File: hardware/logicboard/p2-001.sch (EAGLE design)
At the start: 59 parts, among them IC1 74LS07N, IC11 74LS153D, IC12 LTC485S, IC13 LTC485S, IC2 4066N, J1 MKR, J11 Qwiic, J12 Qwiic, J13 Qwiic, J14 Qwiic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

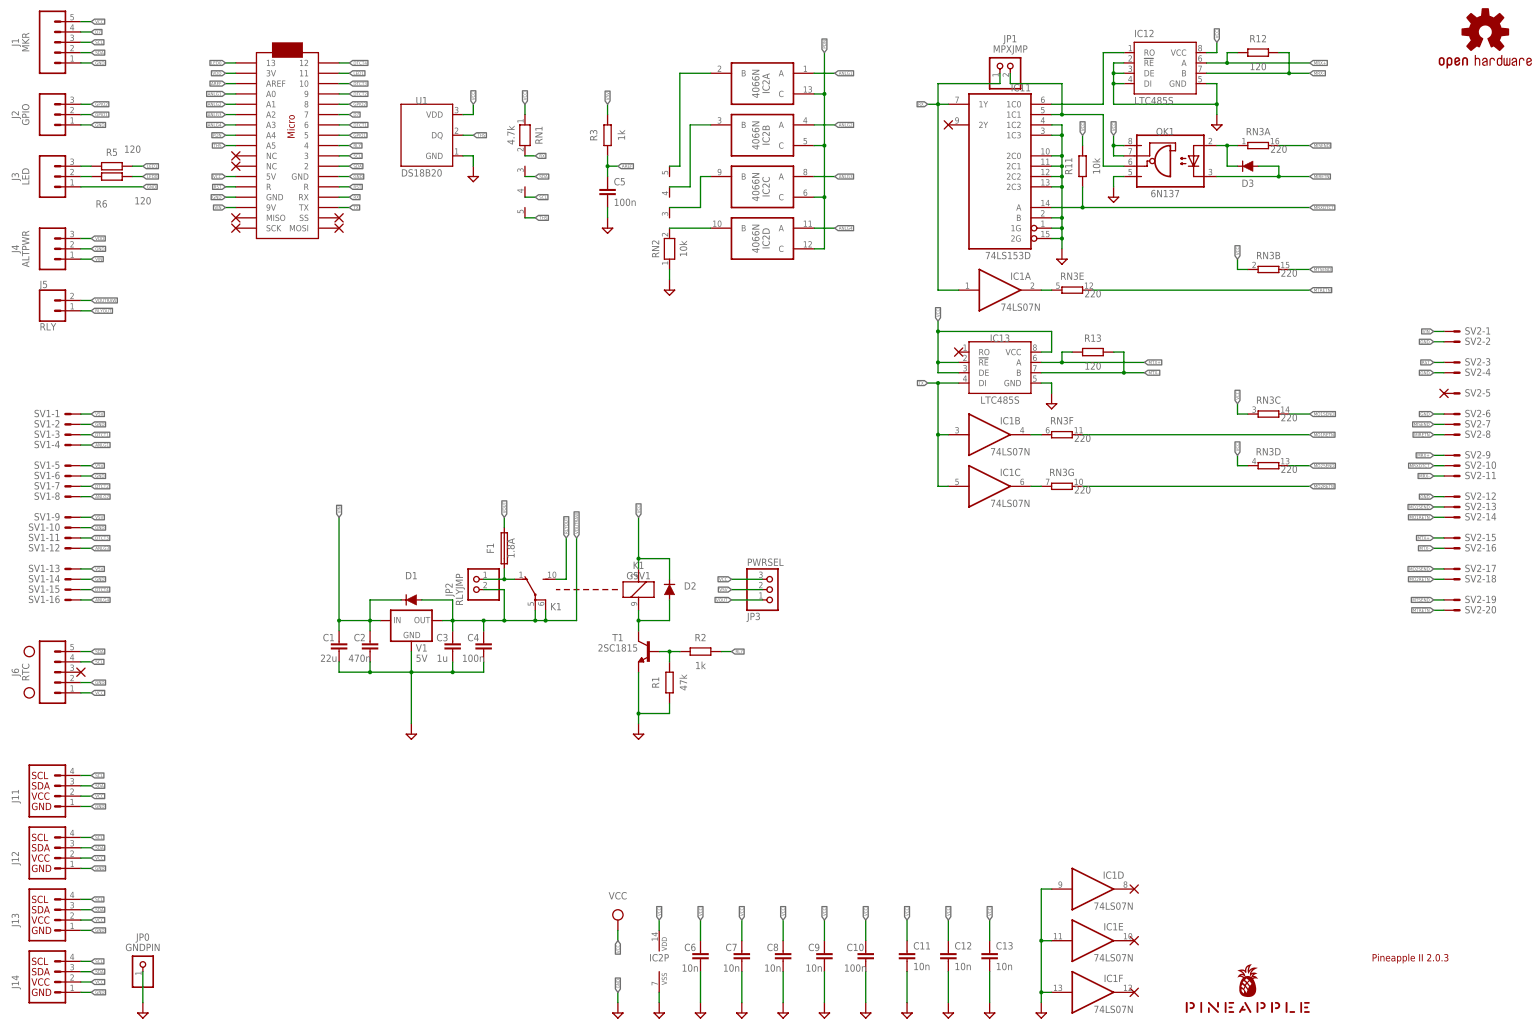
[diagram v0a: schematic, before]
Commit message: Added Power-Grid.
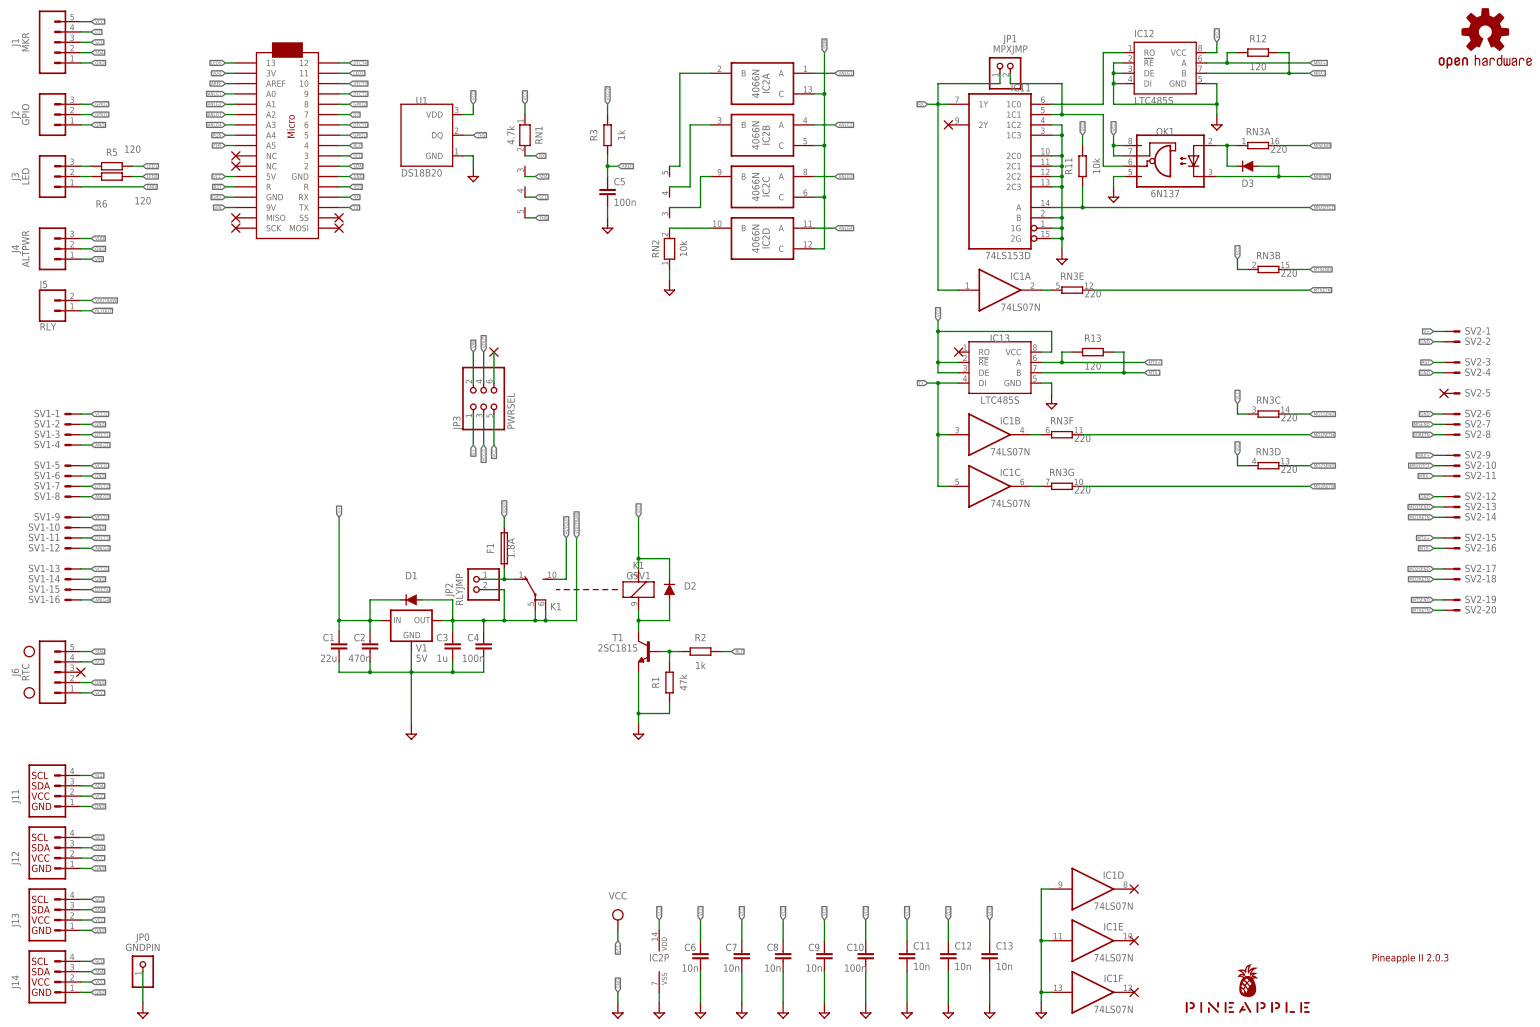
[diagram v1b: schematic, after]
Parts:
- JP3: device pinhead:PINHD-1X3 -> pinhead:PINHD-2X3
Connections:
- removed net V5V: JP3.2, R3.2, SV1-1.S, SV1-13.S, SV1-5.S, SV1-9.S
- new net N$11: JP3.6
- new net V+: C1.1, C2.1, D1.C, JP3.1, SV2-1.S, V1.IN
- new net VCC/2: JP3.3, R3.2, SV1-1.S, SV1-13.S, SV1-5.S, SV1-9.S
- net VCC: now also JP3.5; no longer JP3.3
- net VIN: now also JP3.2; no longer C1.1, C2.1, D1.C, SV2-1.S, V1.IN
- net VOUT: now also JP3.4; no longer JP3.1
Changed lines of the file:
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@@
 <part name="SUPPLY5" library="supply2" library_urn="urn:adsk.eagle:library:372" deviceset="VCC" device=""/>
 <part name="X14" library="wirepad" library_urn="urn:adsk.eagle:library:412" deviceset="PAD-N" device=""/>
-<part name="JP3" library="pinhead" library_urn="urn:adsk.eagle:library:325" deviceset="PINHD-1X3" device="" package3d_urn="urn:adsk.eagle:package:22458/2" value="PWRSEL"/>
 <part name="J5" library="SparkFun-Connectors" library_urn="urn:adsk.eagle:library:513" deviceset="CONN_02" device="JST-PTH-2" package3d_urn="urn:adsk.eagle:package:38053/1" value="RLY"/>
+<part name="JP3" library="pinhead" library_urn="urn:adsk.eagle:library:325" deviceset="PINHD-2X3" device="" package3d_urn="urn:adsk.eagle:package:22462/2" value="PWRSEL"/>
+<part name="X11" library="wirepad" library_urn="urn:adsk.eagle:library:412" deviceset="PAD-N" device=""/>
 </parts>
 <sheets>
@@
 </instance>
 <instance part="X14" gate="G$1" x="25.4" y="91.44" smashed="yes"/>
-<instance part="JP3" gate="A" x="195.58" y="111.76" smashed="yes" rot="MR180">
-<attribute name="NAME" x="189.23" y="106.045" size="1.778" layer="95" rot="MR180"/>
-<attribute name="VALUE" x="189.23" y="119.38" size="1.778" layer="96" rot="MR180"/>
-</instance>
 <instance part="J5" gate="G$1" x="17.78" y="180.34" smashed="yes">
 <attribute name="VALUE" x="15.24" y="175.514" size="1.778" layer="96" font="vector"/>
 <attribute name="NAME" x="15.24" y="185.928" size="1.778" layer="95" font="vector"/>
 </instance>
+<instance part="JP3" gate="A" x="124.46" y="157.48" smashed="yes" rot="R90">
+<attribute name="NAME" x="118.745" y="151.13" size="1.778" layer="95" rot="R90"/>
+<attribute name="VALUE" x="132.08" y="151.13" size="1.778" layer="96" rot="R90"/>
+</instance>
+<instance part="X11" gate="G$1" x="127" y="170.18" smashed="yes"/>
 </instances>
 <busses>
@@
 </segment>
 <segment>
-<pinref part="JP3" gate="A" pin="3"/>
-<wire x1="193.04" y1="114.3" x2="185.42" y2="114.3" width="0.1524" layer="91"/>
-<label x="185.42" y="114.3" size="0.8128" layer="95" rot="MR0" xref="yes"/>
+<pinref part="JP3" gate="A" pin="5"/>
+<wire x1="127" y1="154.94" x2="127" y2="147.32" width="0.1524" layer="91"/>
+<label x="127" y="147.32" size="0.8128" layer="95" rot="R270" xref="yes"/>
 </segment>
 </net>
@@
 <net name="VIN" class="2">
 <segment>
-<pinref part="SV2" gate="-1" pin="S"/>
-<wire x1="358.14" y1="175.26" x2="360.68" y2="175.26" width="0.1524" layer="91"/>
-<label x="358.14" y="175.26" size="0.8128" layer="95" rot="MR0" xref="yes"/>
-</segment>
-<segment>
 <pinref part="J4" gate="J$1" pin="1"/>
 <wire x1="25.4" y1="193.04" x2="27.94" y2="193.04" width="0.1524" layer="91"/>
@@
 </segment>
 <segment>
-<pinref part="V1" gate="A" pin="IN"/>
-<wire x1="99.06" y1="104.14" x2="96.52" y2="104.14" width="0.1524" layer="91"/>
-<pinref part="C1" gate="G$1" pin="1"/>
-<wire x1="96.52" y1="104.14" x2="88.9" y2="104.14" width="0.1524" layer="91"/>
-<wire x1="88.9" y1="104.14" x2="88.9" y2="101.6" width="0.1524" layer="91"/>
-<pinref part="C2" gate="G$1" pin="1"/>
-<wire x1="96.52" y1="101.6" x2="96.52" y2="104.14" width="0.1524" layer="91"/>
-<junction x="96.52" y="104.14"/>
-<wire x1="96.52" y1="104.14" x2="96.52" y2="109.22" width="0.1524" layer="91"/>
-<pinref part="D1" gate="G$1" pin="C"/>
-<wire x1="96.52" y1="109.22" x2="104.14" y2="109.22" width="0.1524" layer="91"/>
-<wire x1="88.9" y1="104.14" x2="88.9" y2="129.54" width="0.1524" layer="91"/>
-<junction x="88.9" y="104.14"/>
-<label x="88.9" y="129.54" size="0.8128" layer="95" rot="R90" xref="yes"/>
-</segment>
-</net>
-<net name="V5V" class="2">
+<pinref part="JP3" gate="A" pin="2"/>
+<wire x1="121.92" y1="162.56" x2="121.92" y2="170.18" width="0.1524" layer="91"/>
+<label x="121.92" y="170.18" size="0.8128" layer="95" rot="R90" xref="yes"/>
+</segment>
+</net>
+<net name="VCC/2" class="2">
 <segment>
 <pinref part="R3" gate="G$1" pin="2"/>
@@
 </segment>
 <segment>
-<pinref part="JP3" gate="A" pin="2"/>
-<wire x1="193.04" y1="111.76" x2="185.42" y2="111.76" width="0.1524" layer="91"/>
-<label x="185.42" y="111.76" size="0.8128" layer="95" rot="MR0" xref="yes"/>
+<pinref part="JP3" gate="A" pin="3"/>
+<wire x1="124.46" y1="154.94" x2="124.46" y2="147.32" width="0.1524" layer="91"/>
+<label x="124.46" y="147.32" size="0.8128" layer="95" rot="R270" xref="yes"/>
 </segment>
 </net>
@@
 </segment>
 <segment>
-<pinref part="JP3" gate="A" pin="1"/>
-<wire x1="193.04" y1="109.22" x2="185.42" y2="109.22" width="0.1524" layer="91"/>
-<label x="185.42" y="109.22" size="0.8128" layer="95" rot="MR0" xref="yes"/>
+<pinref part="JP3" gate="A" pin="4"/>
+<wire x1="124.46" y1="162.56" x2="124.46" y2="170.18" width="0.1524" layer="91"/>
+<label x="124.46" y="170.18" size="0.8128" layer="95" rot="R90" xref="yes"/>
 </segment>
 </net>
@@
 </segment>
 </net>
+<net name="V+" class="2">
+<segment>
+<pinref part="V1" gate="A" pin="IN"/>
+<wire x1="99.06" y1="104.14" x2="96.52" y2="104.14" width="0.1524" layer="91"/>
+<pinref part="C1" gate="G$1" pin="1"/>
+<wire x1="96.52" y1="104.14" x2="88.9" y2="104.14" width="0.1524" layer="91"/>
+<wire x1="88.9" y1="104.14" x2="88.9" y2="101.6" width="0.1524" layer="91"/>
+<pinref part="C2" gate="G$1" pin="1"/>
+<wire x1="96.52" y1="101.6" x2="96.52" y2="104.14" width="0.1524" layer="91"/>
+<junction x="96.52" y="104.14"/>
+<wire x1="96.52" y1="104.14" x2="96.52" y2="109.22" width="0.1524" layer="91"/>
+<pinref part="D1" gate="G$1" pin="C"/>
+<wire x1="96.52" y1="109.22" x2="104.14" y2="109.22" width="0.1524" layer="91"/>
+<wire x1="88.9" y1="104.14" x2="88.9" y2="129.54" width="0.1524" layer="91"/>
+<junction x="88.9" y="104.14"/>
+<label x="88.9" y="129.54" size="0.8128" layer="95" rot="R90" xref="yes"/>
+</segment>
+<segment>
+<pinref part="SV2" gate="-1" pin="S"/>
+<wire x1="358.14" y1="175.26" x2="360.68" y2="175.26" width="0.1524" layer="91"/>
+<label x="358.14" y="175.26" size="0.8128" layer="95" rot="MR0" xref="yes"/>
+</segment>
+<segment>
+<pinref part="JP3" gate="A" pin="1"/>
+<wire x1="121.92" y1="154.94" x2="121.92" y2="147.32" width="0.1524" layer="91"/>
+<label x="121.92" y="147.32" size="0.8128" layer="95" rot="R270" xref="yes"/>
+</segment>
+</net>
+<net name="N$11" class="0">
+<segment>
+<pinref part="JP3" gate="A" pin="6"/>
+<wire x1="127" y1="162.56" x2="127" y2="170.18" width="0.1524" layer="91"/>
+</segment>
+</net>

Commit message: Power Grid 2.
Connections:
- removed net N$11: JP3.6
- net VOUT: now also JP3.6
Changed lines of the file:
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@@
 <part name="J5" library="SparkFun-Connectors" library_urn="urn:adsk.eagle:library:513" deviceset="CONN_02" device="JST-PTH-2" package3d_urn="urn:adsk.eagle:package:38053/1" value="RLY"/>
 <part name="JP3" library="pinhead" library_urn="urn:adsk.eagle:library:325" deviceset="PINHD-2X3" device="" package3d_urn="urn:adsk.eagle:package:22462/2" value="PWRSEL"/>
-<part name="X11" library="wirepad" library_urn="urn:adsk.eagle:library:412" deviceset="PAD-N" device=""/>
 </parts>
 <sheets>
@@
 <attribute name="VALUE" x="132.08" y="151.13" size="1.778" layer="96" rot="R90"/>
 </instance>
-<instance part="X11" gate="G$1" x="127" y="170.18" smashed="yes"/>
 </instances>
 <busses>
@@
 <label x="124.46" y="170.18" size="0.8128" layer="95" rot="R90" xref="yes"/>
 </segment>
+<segment>
+<pinref part="JP3" gate="A" pin="6"/>
+<wire x1="127" y1="162.56" x2="127" y2="170.18" width="0.1524" layer="91"/>
+<label x="127" y="170.18" size="0.8128" layer="95" rot="R90" xref="yes"/>
+</segment>
 </net>
 <net name="VOUTRAW" class="2">
@@
 </segment>
 </net>
-<net name="N$11" class="0">
-<segment>
-<pinref part="JP3" gate="A" pin="6"/>
-<wire x1="127" y1="162.56" x2="127" y2="170.18" width="0.1524" layer="91"/>
-</segment>
-</net>

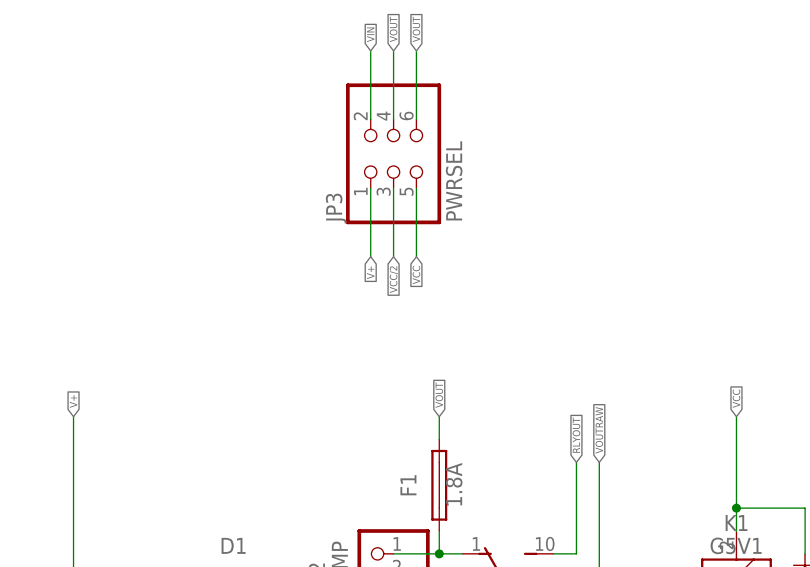
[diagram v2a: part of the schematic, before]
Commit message: Swapped Vcc and Vcc/2.
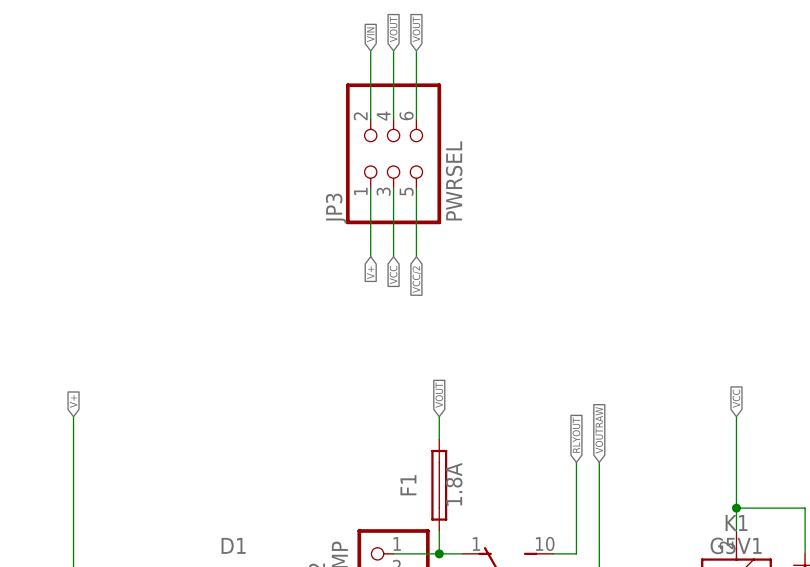
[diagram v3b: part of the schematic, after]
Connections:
- net VCC: now also JP3.3; no longer JP3.5
- net VCC/2: now also JP3.5; no longer JP3.3
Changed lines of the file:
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@@
 </segment>
 <segment>
-<pinref part="JP3" gate="A" pin="5"/>
-<wire x1="127" y1="154.94" x2="127" y2="147.32" width="0.1524" layer="91"/>
-<label x="127" y="147.32" size="0.8128" layer="95" rot="R270" xref="yes"/>
+<pinref part="JP3" gate="A" pin="3"/>
+<wire x1="124.46" y1="154.94" x2="124.46" y2="147.32" width="0.1524" layer="91"/>
+<label x="124.46" y="147.32" size="0.8128" layer="95" rot="R270" xref="yes"/>
 </segment>
 </net>
@@
 </segment>
 <segment>
-<pinref part="JP3" gate="A" pin="3"/>
-<wire x1="124.46" y1="154.94" x2="124.46" y2="147.32" width="0.1524" layer="91"/>
-<label x="124.46" y="147.32" size="0.8128" layer="95" rot="R270" xref="yes"/>
-</segment>
-</net>
+<pinref part="JP3" gate="A" pin="5"/>
+<wire x1="127" y1="154.94" x2="127" y2="147.32" width="0.1524" layer="91"/>
+<label x="127" y="147.32" size="0.8128" layer="95" rot="R270" xref="yes"/>
+</segment>
+</net>

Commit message: Fixed some errors.
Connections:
- net N$4 renamed VOUTRAW2
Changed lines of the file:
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@@
 </segment>
 </net>
-<net name="N$4" class="0">
+<net name="VOUTRAW2" class="2">
 <segment>
 <pinref part="F1" gate="1" pin="1"/>
